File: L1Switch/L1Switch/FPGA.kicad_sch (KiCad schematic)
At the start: 34 parts, among them J11 Conn_01x06_Male, U1 XC7A35T-FTG256, X1 LFSPXO076034CUTT

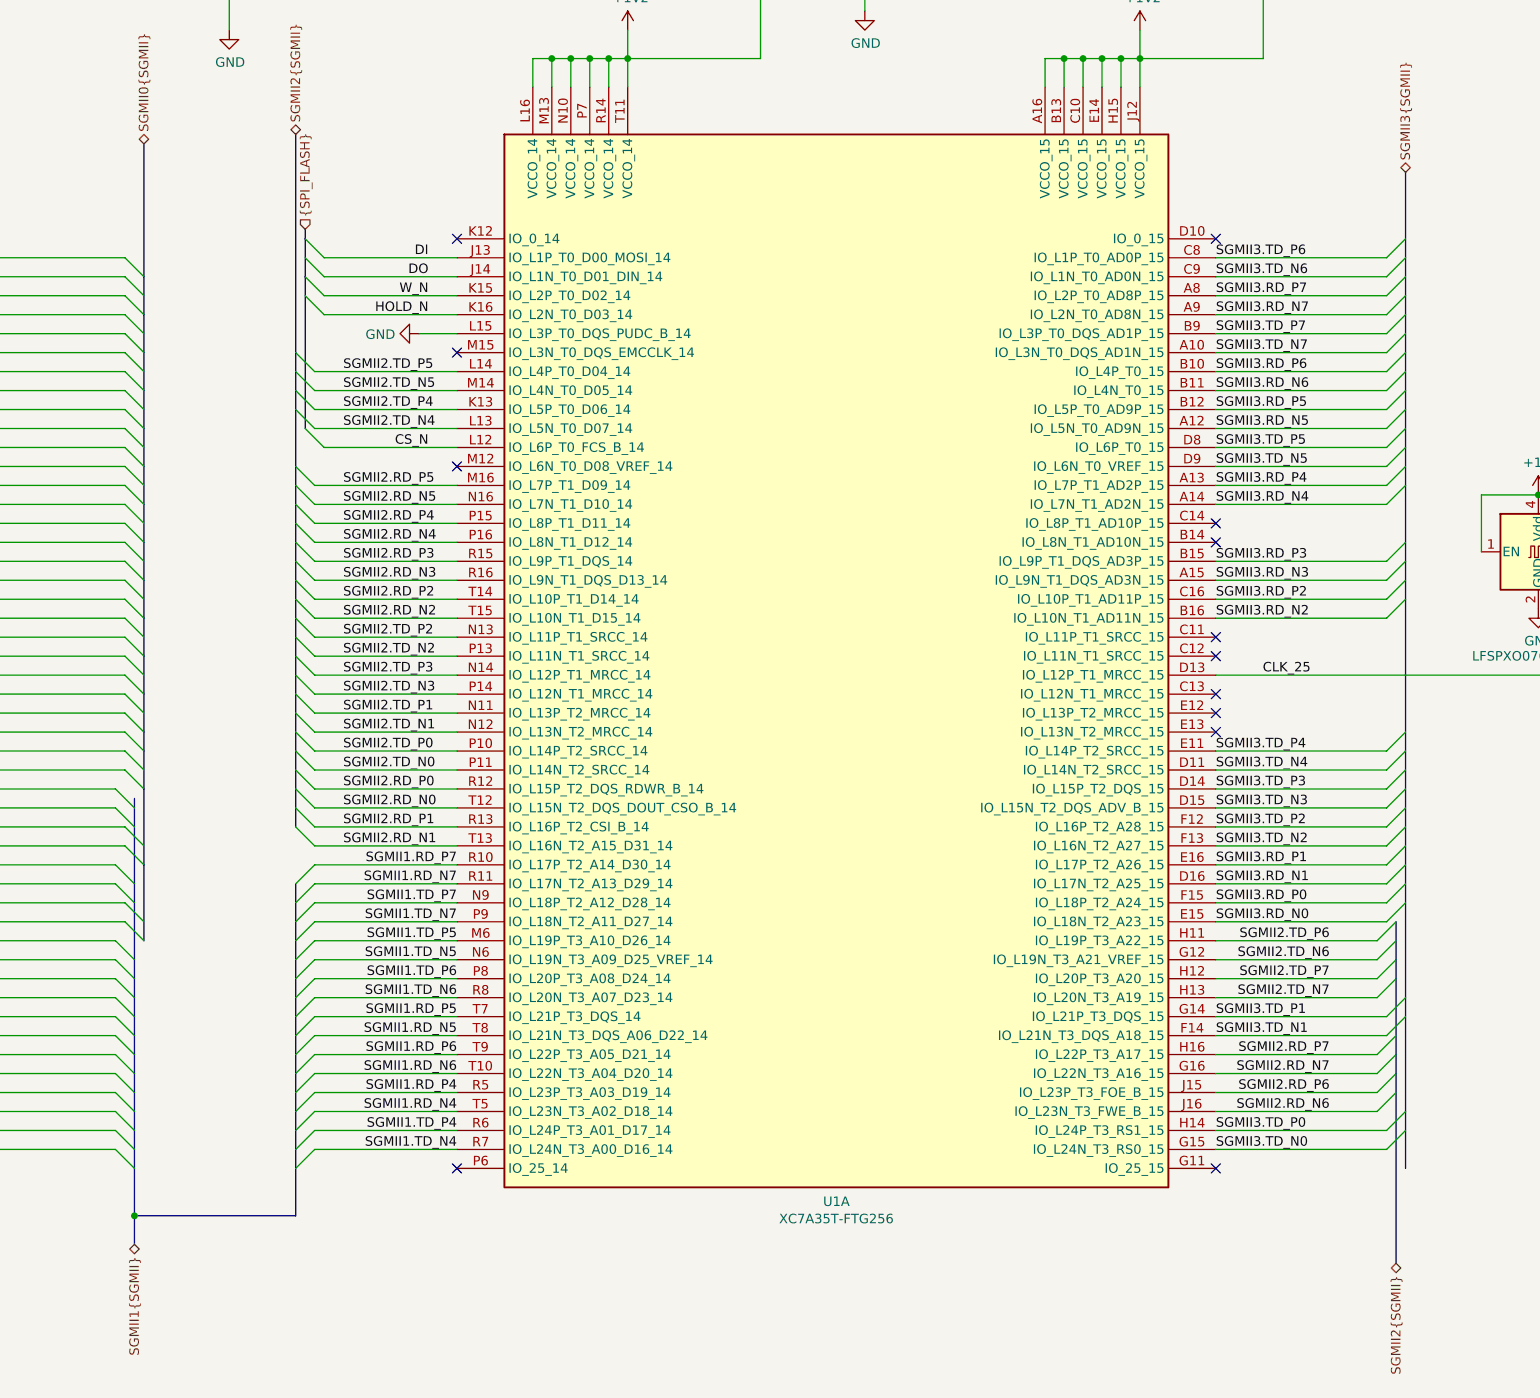
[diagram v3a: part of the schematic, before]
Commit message: Update voltage monitoring.
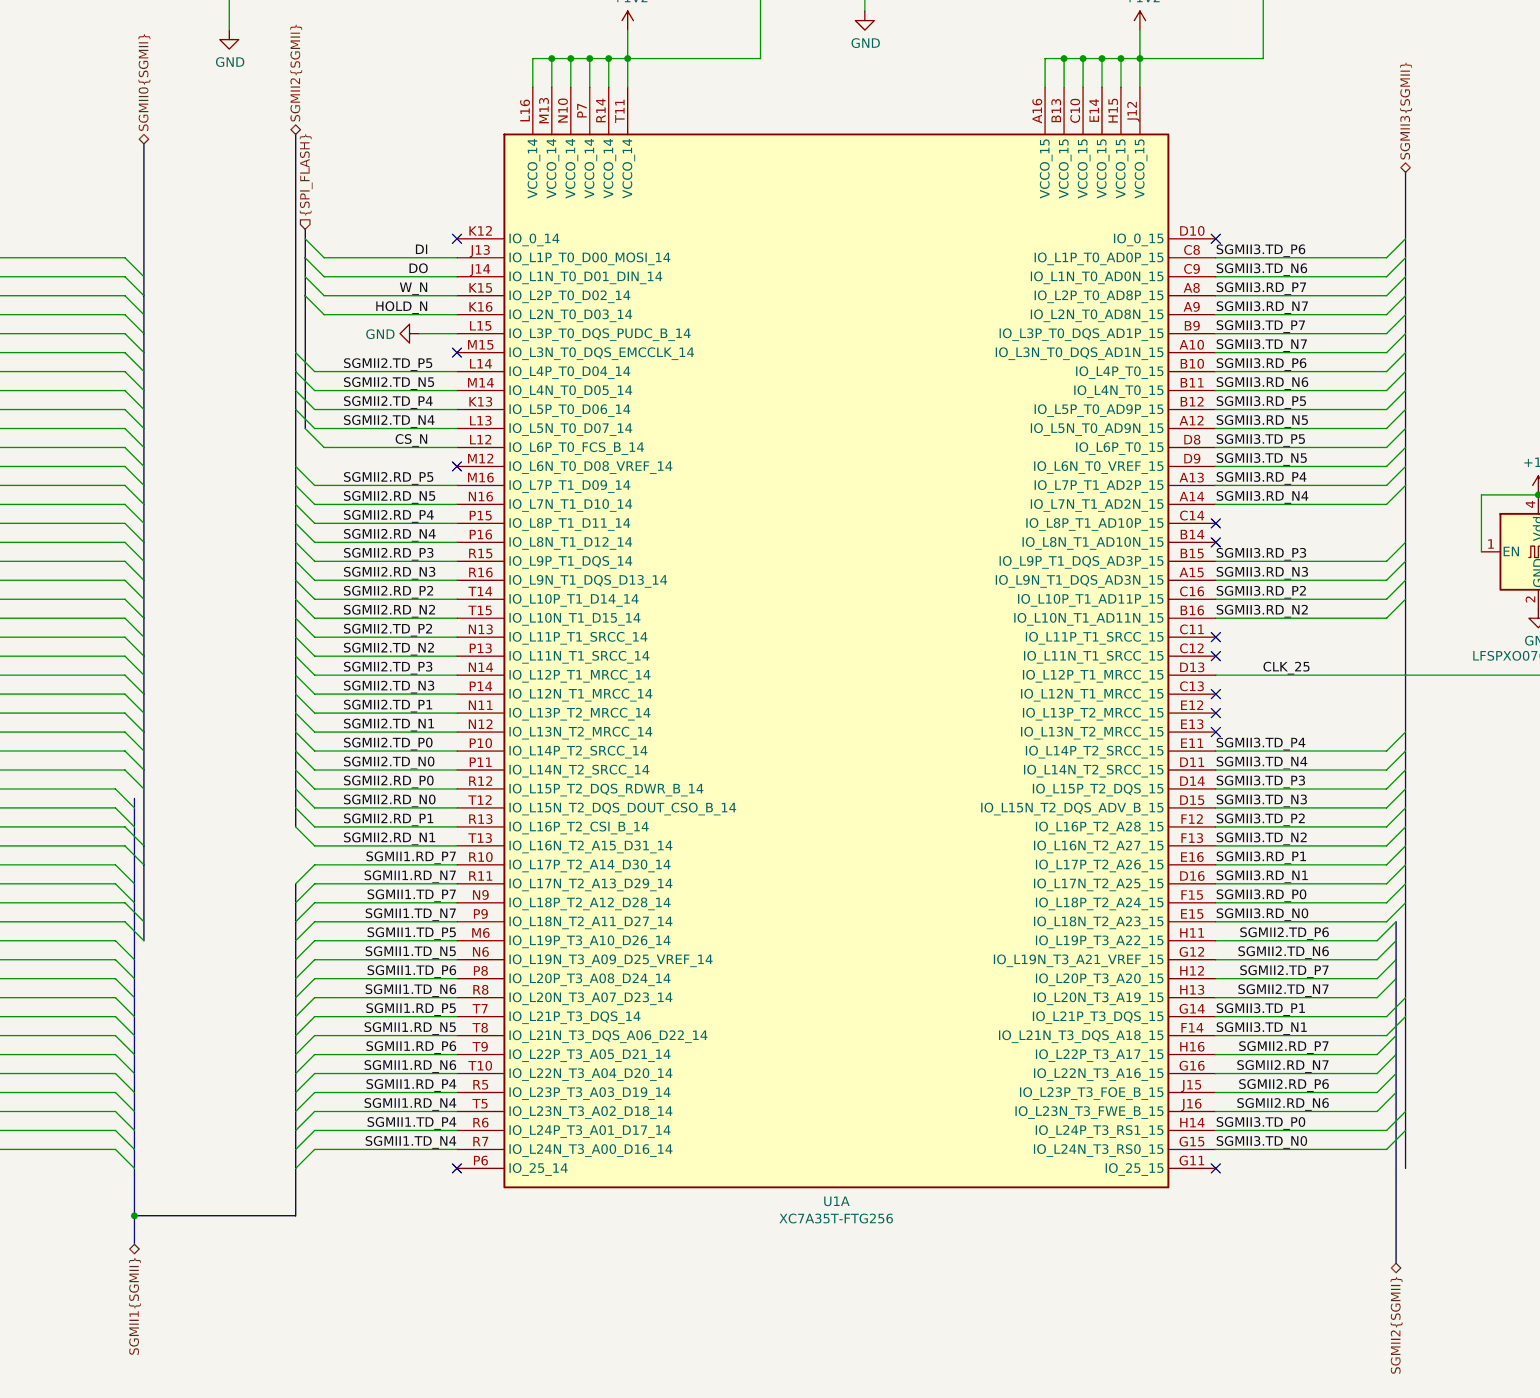
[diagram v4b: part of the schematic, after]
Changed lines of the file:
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@@
   (junction (at 414.02 125.73))
   (junction (at 213.36 198.12))
-  (no_connect (at 256.54 191.77))
+  (no_connect (at 358.14 67.31))
+  (no_connect (at 256.54 97.79))
+  (no_connect (at 358.14 120.65))
+  (no_connect (at 46.99 114.3))
+  (no_connect (at 358.14 128.27))
+  (no_connect (at 76.2 105.41))
+  (no_connect (at 177.8 191.77))
+  (no_connect (at 46.99 116.84))
+  (no_connect (at 358.14 105.41))
+  (no_connect (at 177.8 67.31))
+  (no_connect (at 256.54 67.31))
+  (no_connect (at 358.14 107.95))
+  (no_connect (at 358.14 133.35))
+  (no_connect (at 46.99 124.46))
   (no_connect (at 256.54 82.55))
   (no_connect (at 76.2 115.57))
+  (no_connect (at 76.2 102.87))
+  (no_connect (at 76.2 107.95))
   (no_connect (at 358.14 191.77))
-  (no_connect (at 46.99 116.84))
-  (no_connect (at 358.14 128.27))
-  (no_connect (at 76.2 107.95))
-  (no_connect (at 256.54 67.31))
+  (no_connect (at 256.54 191.77))
   (no_connect (at 358.14 123.19))
-  (no_connect (at 358.14 105.41))
-  (no_connect (at 177.8 191.77))
-  (no_connect (at 177.8 67.31))
-  (no_connect (at 46.99 124.46))
-  (no_connect (at 358.14 120.65))
-  (no_connect (at 358.14 67.31))
-  (no_connect (at 46.99 114.3))
-  (no_connect (at 256.54 97.79))
-  (no_connect (at 358.14 107.95))
   (no_connect (at 358.14 130.81))
-  (no_connect (at 76.2 105.41))
-  (no_connect (at 358.14 133.35))
-  (no_connect (at 76.2 102.87))
   (bus_entry (at 210.82 140.97) (size 2.54 2.54))
   (bus_entry (at 210.82 143.51) (size 2.54 2.54))
@@
     (stroke (width 0) (type solid) (color 0 0 0 0))
   )
-  (bus (pts (xy 213.36 184.15) (xy 213.36 186.69))
-    (stroke (width 0) (type solid) (color 0 0 0 0))
-  )
-  (bus (pts (xy 213.36 186.69) (xy 213.36 191.77))
-    (stroke (width 0) (type solid) (color 0 0 0 0))
-  )
-  (bus (pts (xy 213.36 191.77) (xy 213.36 198.12))
+  (bus (pts (xy 213.36 184.15) (xy 213.36 189.23))
+    (stroke (width 0) (type solid) (color 0 0 0 0))
+  )
+  (bus (pts (xy 213.36 189.23) (xy 213.36 198.12))
     (stroke (width 0) (type solid) (color 0 0 0 0))
   )
@@
     (stroke (width 0) (type solid) (color 0 0 0 0))
   )
-  (bus (pts (xy 214.63 54.61) (xy 214.63 72.39))
-    (stroke (width 0) (type solid) (color 0 0 0 0))
-  )
-  (bus (pts (xy 214.63 72.39) (xy 214.63 77.47))
-    (stroke (width 0) (type solid) (color 0 0 0 0))
-  )
-  (bus (pts (xy 214.63 77.47) (xy 214.63 82.55))
+  (bus (pts (xy 214.63 54.61) (xy 214.63 74.93))
+    (stroke (width 0) (type solid) (color 0 0 0 0))
+  )
+  (bus (pts (xy 214.63 74.93) (xy 214.63 80.01))
+    (stroke (width 0) (type solid) (color 0 0 0 0))
+  )
+  (bus (pts (xy 214.63 80.01) (xy 214.63 82.55))
     (stroke (width 0) (type solid) (color 0 0 0 0))
   )
@@
     (stroke (width 0) (type solid) (color 0 0 0 0))
   )
-  (bus (pts (xy 214.63 92.71) (xy 214.63 97.79))
-    (stroke (width 0) (type solid) (color 0 0 0 0))
-  )
-  (bus (pts (xy 214.63 97.79) (xy 214.63 102.87))
+  (bus (pts (xy 214.63 92.71) (xy 214.63 95.25))
+    (stroke (width 0) (type solid) (color 0 0 0 0))
+  )
+  (bus (pts (xy 214.63 95.25) (xy 214.63 100.33))
+    (stroke (width 0) (type solid) (color 0 0 0 0))
+  )
+  (bus (pts (xy 214.63 100.33) (xy 214.63 102.87))
     (stroke (width 0) (type solid) (color 0 0 0 0))
   )
@@
     (stroke (width 0) (type solid) (color 0 0 0 0))
   )
-  (bus (pts (xy 214.63 133.35) (xy 214.63 135.89))
-    (stroke (width 0) (type solid) (color 0 0 0 0))
-  )
-  (bus (pts (xy 214.63 135.89) (xy 214.63 140.97))
-    (stroke (width 0) (type solid) (color 0 0 0 0))
-  )
-  (bus (pts (xy 214.63 140.97) (xy 214.63 151.13))
+  (bus (pts (xy 214.63 133.35) (xy 214.63 138.43))
+    (stroke (width 0) (type solid) (color 0 0 0 0))
+  )
+  (bus (pts (xy 214.63 138.43) (xy 214.63 148.59))
+    (stroke (width 0) (type solid) (color 0 0 0 0))
+  )
+  (bus (pts (xy 214.63 148.59) (xy 214.63 151.13))
     (stroke (width 0) (type solid) (color 0 0 0 0))
   )
@@
     (stroke (width 0) (type solid) (color 0 0 0 0))
   )
-  (bus (pts (xy 234.95 53.34) (xy 234.95 82.55))
-    (stroke (width 0) (type solid) (color 0 0 0 0))
-  )
-  (bus (pts (xy 234.95 82.55) (xy 234.95 87.63))
-    (stroke (width 0) (type solid) (color 0 0 0 0))
-  )
-  (bus (pts (xy 234.95 87.63) (xy 234.95 97.79))
-    (stroke (width 0) (type solid) (color 0 0 0 0))
-  )
-  (bus (pts (xy 234.95 97.79) (xy 234.95 100.33))
+  (bus (pts (xy 234.95 53.34) (xy 234.95 85.09))
+    (stroke (width 0) (type solid) (color 0 0 0 0))
+  )
+  (bus (pts (xy 234.95 85.09) (xy 234.95 90.17))
+    (stroke (width 0) (type solid) (color 0 0 0 0))
+  )
+  (bus (pts (xy 234.95 90.17) (xy 234.95 100.33))
     (stroke (width 0) (type solid) (color 0 0 0 0))
   )
@@
     (stroke (width 0) (type solid) (color 0 0 0 0))
   )
-  (bus (pts (xy 234.95 110.49) (xy 234.95 115.57))
-    (stroke (width 0) (type solid) (color 0 0 0 0))
-  )
-  (bus (pts (xy 234.95 115.57) (xy 234.95 120.65))
-    (stroke (width 0) (type solid) (color 0 0 0 0))
-  )
-  (bus (pts (xy 234.95 120.65) (xy 234.95 125.73))
+  (bus (pts (xy 234.95 110.49) (xy 234.95 113.03))
+    (stroke (width 0) (type solid) (color 0 0 0 0))
+  )
+  (bus (pts (xy 234.95 113.03) (xy 234.95 118.11))
+    (stroke (width 0) (type solid) (color 0 0 0 0))
+  )
+  (bus (pts (xy 234.95 118.11) (xy 234.95 123.19))
+    (stroke (width 0) (type solid) (color 0 0 0 0))
+  )
+  (bus (pts (xy 234.95 123.19) (xy 234.95 125.73))
     (stroke (width 0) (type solid) (color 0 0 0 0))
   )
@@
     (stroke (width 0) (type solid) (color 0 0 0 0))
   )
-  (bus (pts (xy 234.95 158.75) (xy 234.95 161.29))
-    (stroke (width 0) (type solid) (color 0 0 0 0))
-  )
-  (bus (pts (xy 234.95 161.29) (xy 234.95 166.37))
-    (stroke (width 0) (type solid) (color 0 0 0 0))
-  )
-  (bus (pts (xy 234.95 166.37) (xy 234.95 168.91))
-    (stroke (width 0) (type solid) (color 0 0 0 0))
-  )
-  (bus (pts (xy 234.95 168.91) (xy 234.95 173.99))
+  (bus (pts (xy 234.95 158.75) (xy 234.95 163.83))
+    (stroke (width 0) (type solid) (color 0 0 0 0))
+  )
+  (bus (pts (xy 234.95 163.83) (xy 234.95 166.37))
+    (stroke (width 0) (type solid) (color 0 0 0 0))
+  )
+  (bus (pts (xy 234.95 166.37) (xy 234.95 171.45))
+    (stroke (width 0) (type solid) (color 0 0 0 0))
+  )
+  (bus (pts (xy 234.95 171.45) (xy 234.95 173.99))
     (stroke (width 0) (type solid) (color 0 0 0 0))
   )
@@
     (stroke (width 0) (type solid) (color 0 0 0 0))
   )
-  (bus (pts (xy 234.95 179.07) (xy 234.95 184.15))
-    (stroke (width 0) (type solid) (color 0 0 0 0))
-  )
-  (bus (pts (xy 234.95 184.15) (xy 234.95 189.23))
-    (stroke (width 0) (type solid) (color 0 0 0 0))
-  )
-  (bus (pts (xy 234.95 189.23) (xy 234.95 198.12))
-    (stroke (width 0) (type solid) (color 0 0 0 0))
-  )
-  (bus (pts (xy 236.22 66.04) (xy 236.22 67.31))
-    (stroke (width 0) (type solid) (color 0 0 0 0))
-  )
-  (bus (pts (xy 236.22 67.31) (xy 236.22 72.39))
-    (stroke (width 0) (type solid) (color 0 0 0 0))
-  )
-  (bus (pts (xy 236.22 72.39) (xy 236.22 92.71))
+  (bus (pts (xy 234.95 179.07) (xy 234.95 181.61))
+    (stroke (width 0) (type solid) (color 0 0 0 0))
+  )
+  (bus (pts (xy 234.95 181.61) (xy 234.95 186.69))
+    (stroke (width 0) (type solid) (color 0 0 0 0))
+  )
+  (bus (pts (xy 234.95 186.69) (xy 234.95 191.77))
+    (stroke (width 0) (type solid) (color 0 0 0 0))
+  )
+  (bus (pts (xy 234.95 191.77) (xy 234.95 198.12))
+    (stroke (width 0) (type solid) (color 0 0 0 0))
+  )
+  (bus (pts (xy 236.22 66.04) (xy 236.22 69.85))
+    (stroke (width 0) (type solid) (color 0 0 0 0))
+  )
+  (bus (pts (xy 236.22 69.85) (xy 236.22 74.93))
+    (stroke (width 0) (type solid) (color 0 0 0 0))
+  )
+  (bus (pts (xy 236.22 74.93) (xy 236.22 92.71))
     (stroke (width 0) (type solid) (color 0 0 0 0))
   )
@@
     (stroke (width 0) (type solid) (color 0 0 0 0))
   )
-  (bus (pts (xy 382.27 176.53) (xy 382.27 179.07))
-    (stroke (width 0) (type solid) (color 0 0 0 0))
-  )
-  (bus (pts (xy 382.27 179.07) (xy 382.27 204.47))
+  (bus (pts (xy 382.27 176.53) (xy 382.27 181.61))
+    (stroke (width 0) (type solid) (color 0 0 0 0))
+  )
+  (bus (pts (xy 382.27 181.61) (xy 382.27 204.47))
     (stroke (width 0) (type solid) (color 0 0 0 0))
   )
@@
     (stroke (width 0) (type solid) (color 0 0 0 0))
   )
-  (bus (pts (xy 383.54 140.97) (xy 383.54 146.05))
-    (stroke (width 0) (type solid) (color 0 0 0 0))
-  )
-  (bus (pts (xy 383.54 146.05) (xy 383.54 151.13))
-    (stroke (width 0) (type solid) (color 0 0 0 0))
-  )
-  (bus (pts (xy 383.54 151.13) (xy 383.54 153.67))
-    (stroke (width 0) (type solid) (color 0 0 0 0))
-  )
-  (bus (pts (xy 383.54 153.67) (xy 383.54 168.91))
-    (stroke (width 0) (type solid) (color 0 0 0 0))
-  )
-  (bus (pts (xy 383.54 168.91) (xy 383.54 184.15))
-    (stroke (width 0) (type solid) (color 0 0 0 0))
-  )
-  (bus (pts (xy 383.54 184.15) (xy 383.54 191.77))
-    (stroke (width 0) (type solid) (color 0 0 0 0))
-  )
+  (bus (pts (xy 383.54 140.97) (xy 383.54 143.51))
+    (stroke (width 0) (type solid) (color 0 0 0 0))
+  )
+  (bus (pts (xy 383.54 143.51) (xy 383.54 148.59))
+    (stroke (width 0) (type solid) (color 0 0 0 0))
+  )
+  (bus (pts (xy 383.54 148.59) (xy 383.54 153.67))
+    (stroke (width 0) (type solid) (color 0 0 0 0))
+  )
+  (bus (pts (xy 383.54 153.67) (xy 383.54 156.21))
+    (stroke (width 0) (type solid) (color 0 0 0 0))
+  )
+  (bus (pts (xy 383.54 156.21) (xy 383.54 171.45))
+    (stroke (width 0) (type solid) (color 0 0 0 0))
+  )
+  (bus (pts (xy 383.54 171.45) (xy 383.54 186.69))
+    (stroke (width 0) (type solid) (color 0 0 0 0))
+  )
+  (bus (pts (xy 383.54 186.69) (xy 383.54 191.77))
+    (stroke (width 0) (type solid) (color 0 0 0 0))
+  )
